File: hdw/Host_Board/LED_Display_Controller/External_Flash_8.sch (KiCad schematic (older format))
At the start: 0 parts

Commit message: Wired Micro to external SRAM, copied Flash 8 times
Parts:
- added C?: 0.1uF, symbol LED_Display_Local_Library:C_Custom
- added C?: 10nF, symbol LED_Display_Local_Library:C_Custom
- added C?: 1nF, symbol LED_Display_Local_Library:C_Custom
- added J?: WP8, symbol Connector_Generic:Conn_02x01
- added R? (x6): 10k, symbol Custom_Library:R_Custom
- added R? (x5): 100, symbol Custom_Library:R_Custom
- added U?: SST25PF020B, Housings_SOIC:SOIC-8_3.9x4.9mm_Pitch1.27mm, symbol LED_Display_Local_Library:SST25PF020B
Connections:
- new net: R?.1, R?.2, U?.1 (~CE)
- new net: R?.1, R?.2, U?.2 (SO)
- new net: J?.1 (Pin_1), R?.2, U?.3 (~WP)
- new net: R?.1, R?.1, U?.5 (SI)
- new net: R?.1, R?.1, U?.6 (SCK)
- new net: R?.1, R?.2, U?.7 (~HOLD)
- new net +3V3: C?.1, C?.1, C?.1, R?.1, R?.1, R?.1, U?.8 (VDD)
- new net FLASH_MISO: R?.1
- new net FLASH_MOSI: R?.2
- new net FLASH_SCK: R?.2
- new net GND: C?.2, C?.2, C?.2, J?.2 (Pin_2), R?.2, R?.2, R?.2, U?.4 (VSS)
- new net ~FLASH_CE8: R?.2
- new net ~FLASH_Hold: R?.2

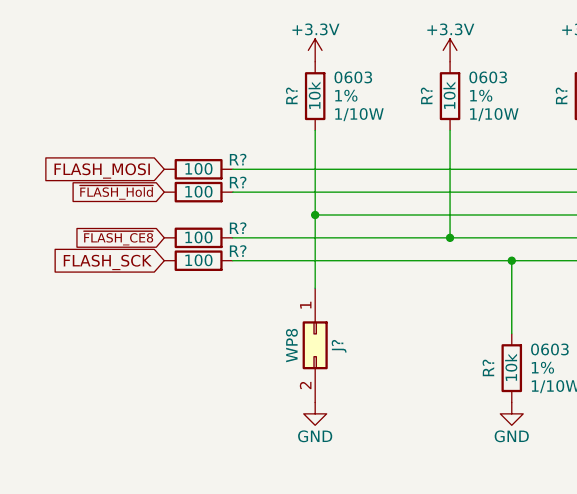
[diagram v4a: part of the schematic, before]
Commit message: Added to-do list, cleaned some pages, ~MCLR filter
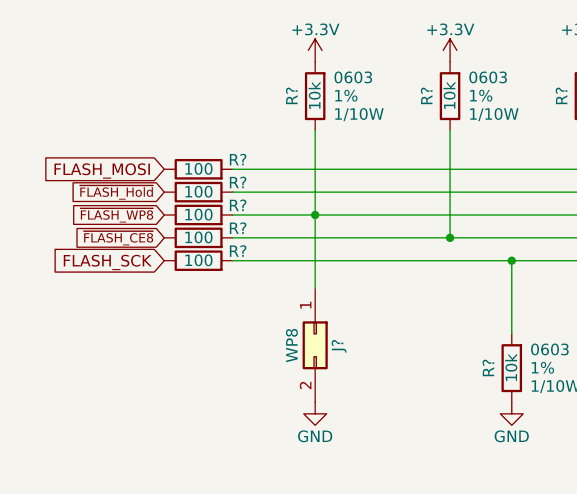
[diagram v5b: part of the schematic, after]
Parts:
- added R?: 100, symbol Custom_Library:R_Custom
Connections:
- net at J?.1 (Pin_1), R?.2, U?.3 (~WP): now also R?.1
- new net ~FLASH_WP8: R?.2
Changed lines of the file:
@@
 $Descr A 11000 8500
 encoding utf-8
-Sheet 23 25
+Sheet 21 25
 Title ""
 Date ""
@@
 AR Path="/5BB181D8/5BBEB738" Ref="C?"  Part="1"
 AR Path="/5BB2595E/5BBEB738" Ref="C?"  Part="1"
+AR Path="/5BB53D67/5BBEB738" Ref="C?"  Part="1"
 F 0 "C?" H 5815 5530 50  0000 L CNN
 F 1 "0.1uF" H 5815 5330 50  0000 L CNN
@@
 AR Path="/5BB181D8/5BBEB743" Ref="C?"  Part="1"
 AR Path="/5BB2595E/5BBEB743" Ref="C?"  Part="1"
+AR Path="/5BB53D67/5BBEB743" Ref="C?"  Part="1"
 F 0 "C?" H 6115 5530 50  0000 L CNN
 F 1 "10nF" H 6115 5330 50  0000 L CNN
@@
 AR Path="/5BB181D8/5BBEB74E" Ref="C?"  Part="1"
 AR Path="/5BB2595E/5BBEB74E" Ref="C?"  Part="1"
+AR Path="/5BB53D67/5BBEB74E" Ref="C?"  Part="1"
 F 0 "C?" H 6415 5530 50  0000 L CNN
 F 1 "1nF" H 6415 5330 50  0000 L CNN
@@
 AR Path="/5BB181D8/5BBEB755" Ref="#PWR?"  Part="1"
 AR Path="/5BB2595E/5BBEB755" Ref="#PWR?"  Part="1"
+AR Path="/5BB53D67/5BBEB755" Ref="#PWR?"  Part="1"
 F 0 "#PWR?" H 6090 5410 50  0001 C CNN
 F 1 "GND" H 6090 5510 50  0000 C CNN
@@
 AR Path="/5BB181D8/5BBEB762" Ref="#PWR?"  Part="1"
 AR Path="/5BB2595E/5BBEB762" Ref="#PWR?"  Part="1"
+AR Path="/5BB53D67/5BBEB762" Ref="#PWR?"  Part="1"
 F 0 "#PWR?" H 6090 5050 50  0001 C CNN
 F 1 "+3.3V" H 6090 5340 50  0000 C CNN
@@
 Text GLabel 3270 3550 0    40   Input ~ 0
 ~FLASH_Hold
+$Comp
+L Custom_Library:R_Custom R?
+U 1 1 5BC205FF
+P 3420 3650
+F 0 "R?" V 3380 3780 50  0000 L CNN
+F 1 "100" V 3420 3650 50  0000 C CNN
+F 2 "" H 3420 3650 50  0001 C CNN
+F 3 "" H 3420 3650 50  0001 C CNN
+F 4 "0603" V 3520 3650 50  0001 C CNN "display_footprint"
+F 5 "1%" V 3620 3650 50  0001 C CNN "Tolerance"
+F 6 "1/10W" V 3720 3650 50  0001 C CNN "Wattage"
+F 7 "PN" H 3720 4050 60  0001 C CNN "Digi-Key PN"
+	1    3420 3650
+	0    1    1    0
+$EndComp
+Wire Wire Line
+	3570 3650 3930 3650
+Text GLabel 3270 3650 0    40   Input ~ 0
+~FLASH_WP8
 $EndSCHEMATC

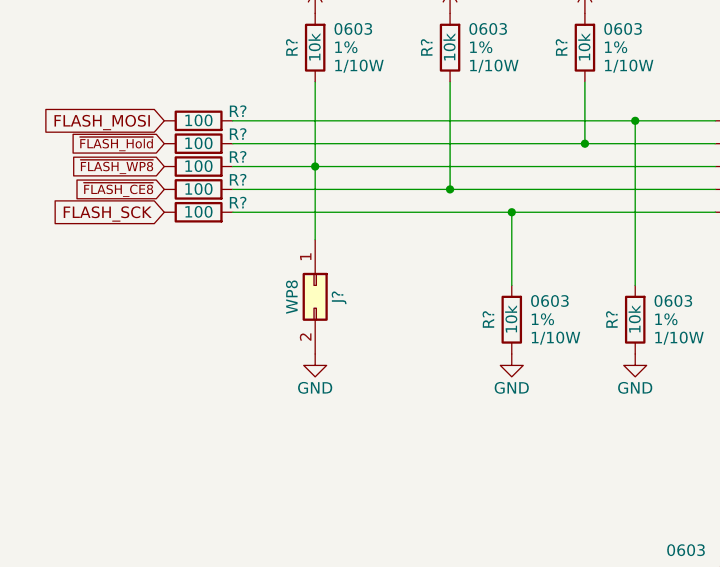
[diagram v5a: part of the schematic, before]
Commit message: Converted to KiCad 5.0.1 project, resolved library issues, cleaned up a few sheets
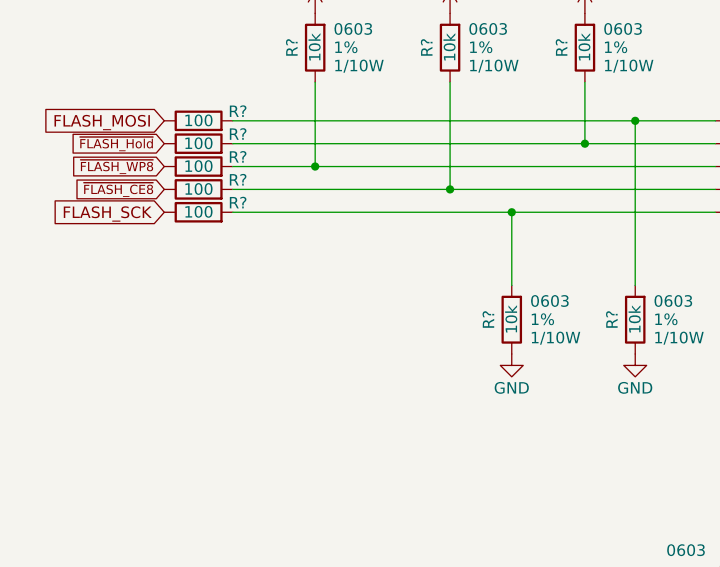
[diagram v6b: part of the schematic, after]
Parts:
- removed J?: WP8, symbol Connector_Generic:Conn_02x01
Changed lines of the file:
@@
 $Descr A 11000 8500
 encoding utf-8
-Sheet 21 25
+Sheet 20 25
 Title ""
 Date ""
@@
 F 3 "" H 6080 4050 50  0001 C CNN
 	1    6080 4050
-	1    0    0    -1
-$EndComp
-$Comp
-L Custom_Library:+3.3V #PWR?
-U 1 1 5BBEB68B
-P 6080 3250
-F 0 "#PWR?" H 6080 3100 50  0001 C CNN
-F 1 "+3.3V" H 6080 3390 50  0000 C CNN
-F 2 "" H 6080 3250 50  0000 C CNN
-F 3 "" H 6080 3250 50  0000 C CNN
-	1    6080 3250
 	1    0    0    -1
 $EndComp
@@
 $EndComp
 $Comp
-L Custom_Library:+3.3V #PWR?
-U 1 1 5BBEB6E5
-P 5110 2980
-F 0 "#PWR?" H 5110 2830 50  0001 C CNN
-F 1 "+3.3V" H 5110 3120 50  0000 C CNN
-F 2 "" H 5110 2980 50  0000 C CNN
-F 3 "" H 5110 2980 50  0000 C CNN
-	1    5110 2980
-	1    0    0    -1
-$EndComp
-$Comp
-L Custom_Library:+3.3V #PWR?
-U 1 1 5BBEB6EB
-P 4520 2980
-F 0 "#PWR?" H 4520 2830 50  0001 C CNN
-F 1 "+3.3V" H 4520 3120 50  0000 C CNN
-F 2 "" H 4520 2980 50  0000 C CNN
-F 3 "" H 4520 2980 50  0000 C CNN
-	1    4520 2980
-	1    0    0    -1
-$EndComp
-$Comp
-L Custom_Library:+3.3V #PWR?
-U 1 1 5BBEB6F1
-P 3930 2980
-F 0 "#PWR?" H 3930 2830 50  0001 C CNN
-F 1 "+3.3V" H 3930 3120 50  0000 C CNN
-F 2 "" H 3930 2980 50  0000 C CNN
-F 3 "" H 3930 2980 50  0000 C CNN
-	1    3930 2980
-	1    0    0    -1
-$EndComp
-$Comp
 L Custom_Library:R_Custom R?
 U 1 1 5BBEB6FB
@@
 Wire Wire Line
 	3930 3650 5680 3650
-$Comp
-L Connector_Generic:Conn_02x01 J?
-U 1 1 5BBEB712
-P 3930 4170
-AR Path="/5BB2595E/5BBEB712" Ref="J?"  Part="1"
-AR Path="/5BB53D67/5BBEB712" Ref="J?"  Part="1"
-F 0 "J?" H 3980 4270 50  0000 C CNN
-F 1 "WP8" H 3980 4070 50  0000 C CNN
-F 2 "" H 3930 4170 50  0001 C CNN
-F 3 "~" H 3930 4170 50  0001 C CNN
-	1    3930 4170
-	0    1    1    0
-$EndComp
-Wire Wire Line
-	3930 3970 3930 3650
 Connection ~ 3930 3650
-$Comp
-L power:GND #PWR?
-U 1 1 5BBEB71B
-P 3930 4470
-F 0 "#PWR?" H 3930 4220 50  0001 C CNN
-F 1 "GND" H 3930 4320 50  0000 C CNN
-F 2 "" H 3930 4470 50  0001 C CNN
-F 3 "" H 3930 4470 50  0001 C CNN
-	1    3930 4470
-	1    0    0    -1
-$EndComp
 Text GLabel 3270 3450 0    50   Input ~ 0
 FLASH_MOSI
@@
 Text GLabel 3270 3650 0    40   Input ~ 0
 ~FLASH_WP8
+$Comp
+L power:+3.3V #PWR?
+U 1 1 5BDFBCCE
+P 3930 2980
+F 0 "#PWR?" H 3930 2830 50  0001 C CNN
+F 1 "+3.3V" H 3930 3120 50  0000 C CNN
+F 2 "" H 3930 2980 50  0001 C CNN
+F 3 "" H 3930 2980 50  0001 C CNN
+	1    3930 2980
+	1    0    0    -1
+$EndComp
+$Comp
+L power:+3.3V #PWR?
+U 1 1 5BDFBD13
+P 4520 2980
+F 0 "#PWR?" H 4520 2830 50  0001 C CNN
+F 1 "+3.3V" H 4520 3120 50  0000 C CNN
+F 2 "" H 4520 2980 50  0001 C CNN
+F 3 "" H 4520 2980 50  0001 C CNN
+	1    4520 2980
+	1    0    0    -1
+$EndComp
+$Comp
+L power:+3.3V #PWR?
+U 1 1 5BDFBD40
+P 5110 2980
+F 0 "#PWR?" H 5110 2830 50  0001 C CNN
+F 1 "+3.3V" H 5110 3120 50  0000 C CNN
+F 2 "" H 5110 2980 50  0001 C CNN
+F 3 "" H 5110 2980 50  0001 C CNN
+	1    5110 2980
+	1    0    0    -1
+$EndComp
+$Comp
+L power:+3.3V #PWR?
+U 1 1 5BDFBD6D
+P 6080 3250
+F 0 "#PWR?" H 6080 3100 50  0001 C CNN
+F 1 "+3.3V" H 6080 3390 50  0000 C CNN
+F 2 "" H 6080 3250 50  0001 C CNN
+F 3 "" H 6080 3250 50  0001 C CNN
+	1    6080 3250
+	1    0    0    -1
+$EndComp
 $EndSCHEMATC
